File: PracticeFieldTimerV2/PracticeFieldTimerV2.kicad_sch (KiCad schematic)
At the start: 21 parts, among them J1 External Controls, J3 Panel, J5 /CAN Enable, J6 RJ45-B, J7 RJ45-A, U1 ESP32-DevKitC

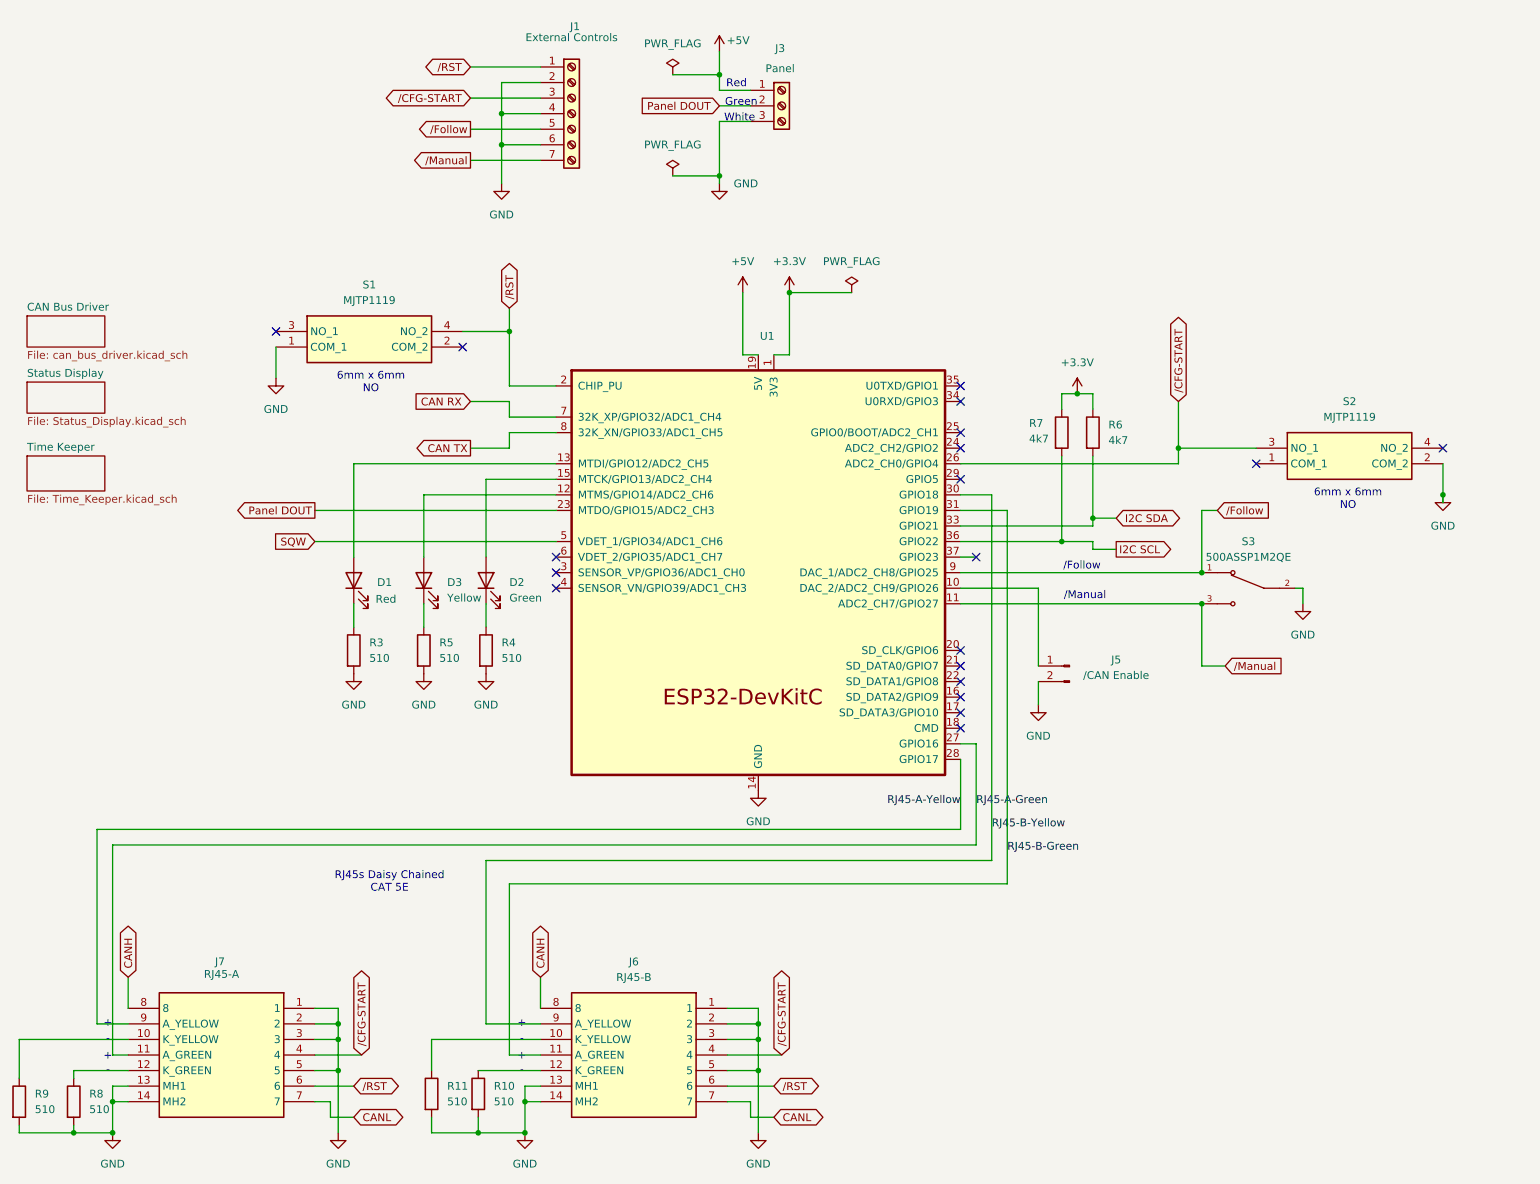
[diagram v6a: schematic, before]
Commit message: Remove on-board LCD Module and I2C->parallel byte converter. Add terminal strip for off-board display. Shrink the board. The board is still a bit spread out, but the changes are significant enough to commit.
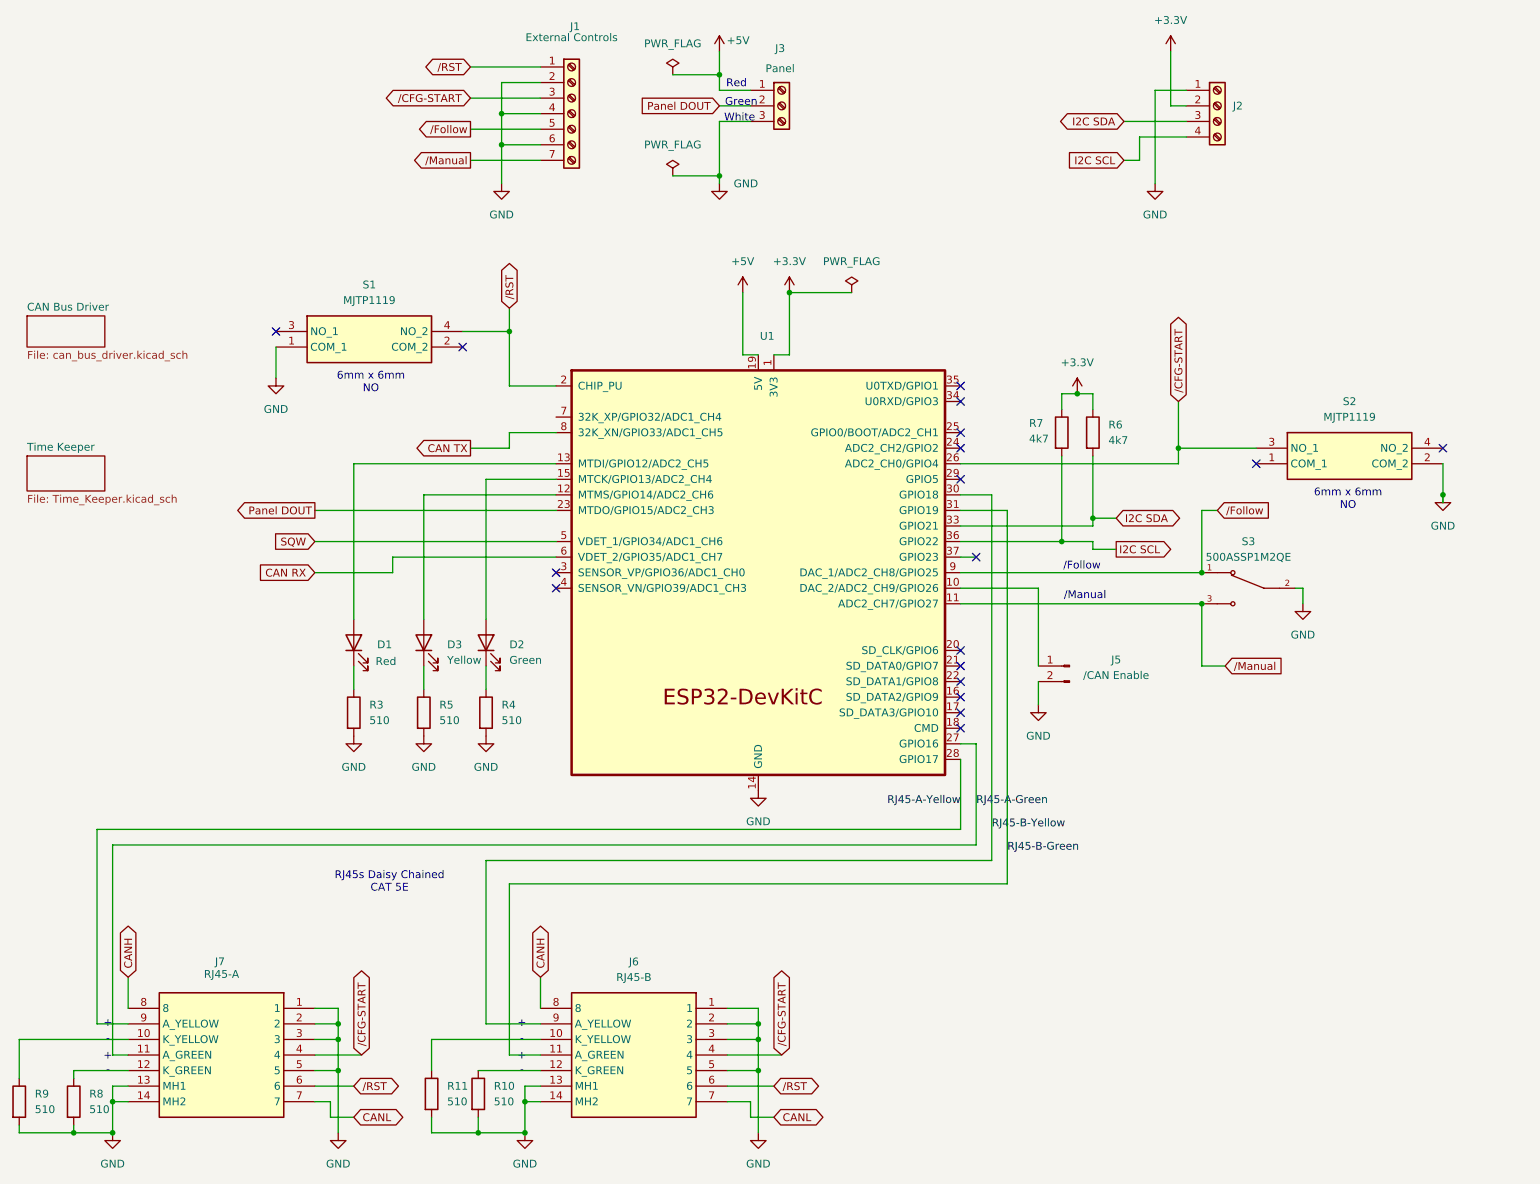
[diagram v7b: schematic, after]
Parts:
- added J2: Screw_Terminal_01x04, TerminalBlock:TerminalBlock_MaiXu_MX126-5.0-04P_1x04_P5.00mm, symbol Connector:Screw_Terminal_01x04
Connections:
- net +3.3V: now also J2.2 (Pin_2)
- net CAN RX: now also U1.6 (VDET_2/GPIO35/ADC1_CH7); no longer U1.7 (32K_XP/GPIO32/ADC1_CH4)
- net GND: now also J2.1 (Pin_1)
- net I2C SCL: now also J2.4 (Pin_4)
- net I2C SDA: now also J2.3 (Pin_3)
- no-connect marks 19 -> 18
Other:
- removed sheet Status Display
- moved on the sheet: D1, D2, D3, R3, R4, R5

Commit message: Tidy the schematic. Ground both common pins on push buttons.
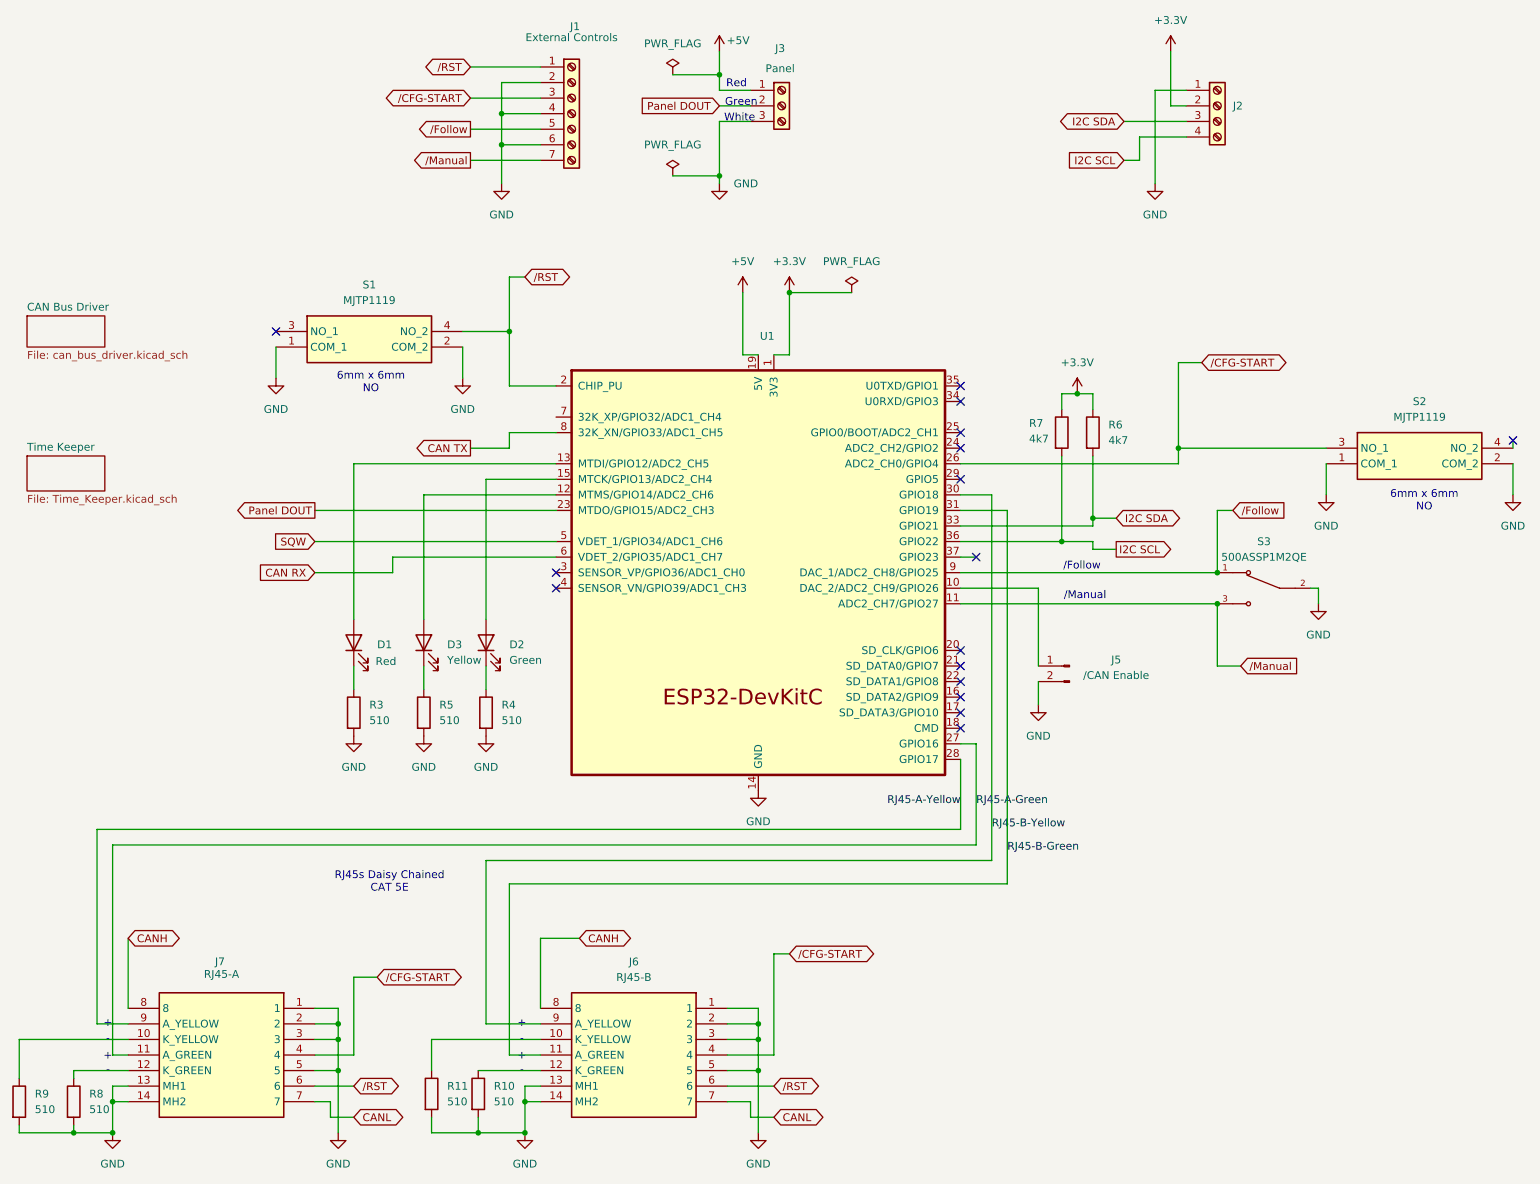
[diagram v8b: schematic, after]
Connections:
- net GND: now also S1.2 (COM_2), S2.1 (COM_1)
- no-connect marks 18 -> 16
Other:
- moved on the sheet: S2, S3
